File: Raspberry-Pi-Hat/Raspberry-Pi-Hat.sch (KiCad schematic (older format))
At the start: 53 parts, among them J3 40HAT, J6 CONN_02X02, J9 CONN_01X02, Q1 DMG2305UX, Q2 DMMT5401, U2 CAT24C32

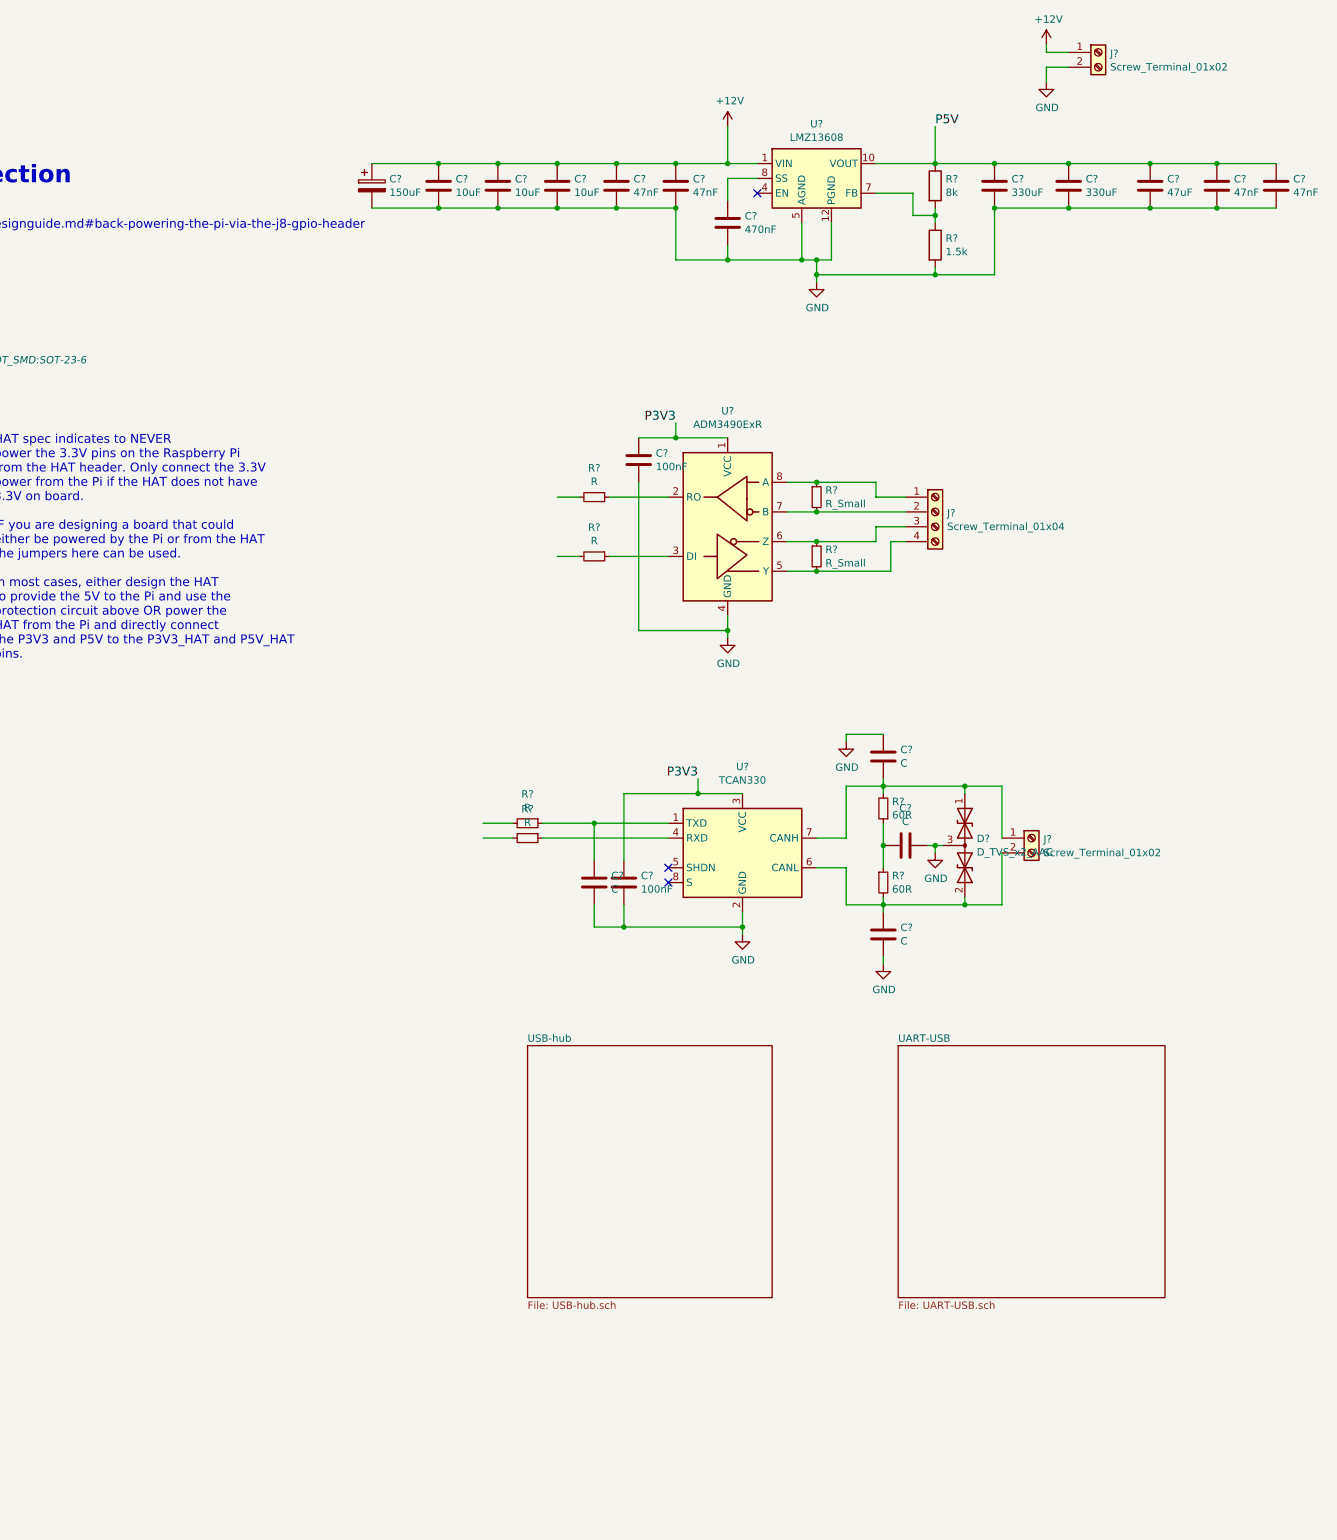
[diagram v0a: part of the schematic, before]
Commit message: USB-HUB
Implementation of USB HUB
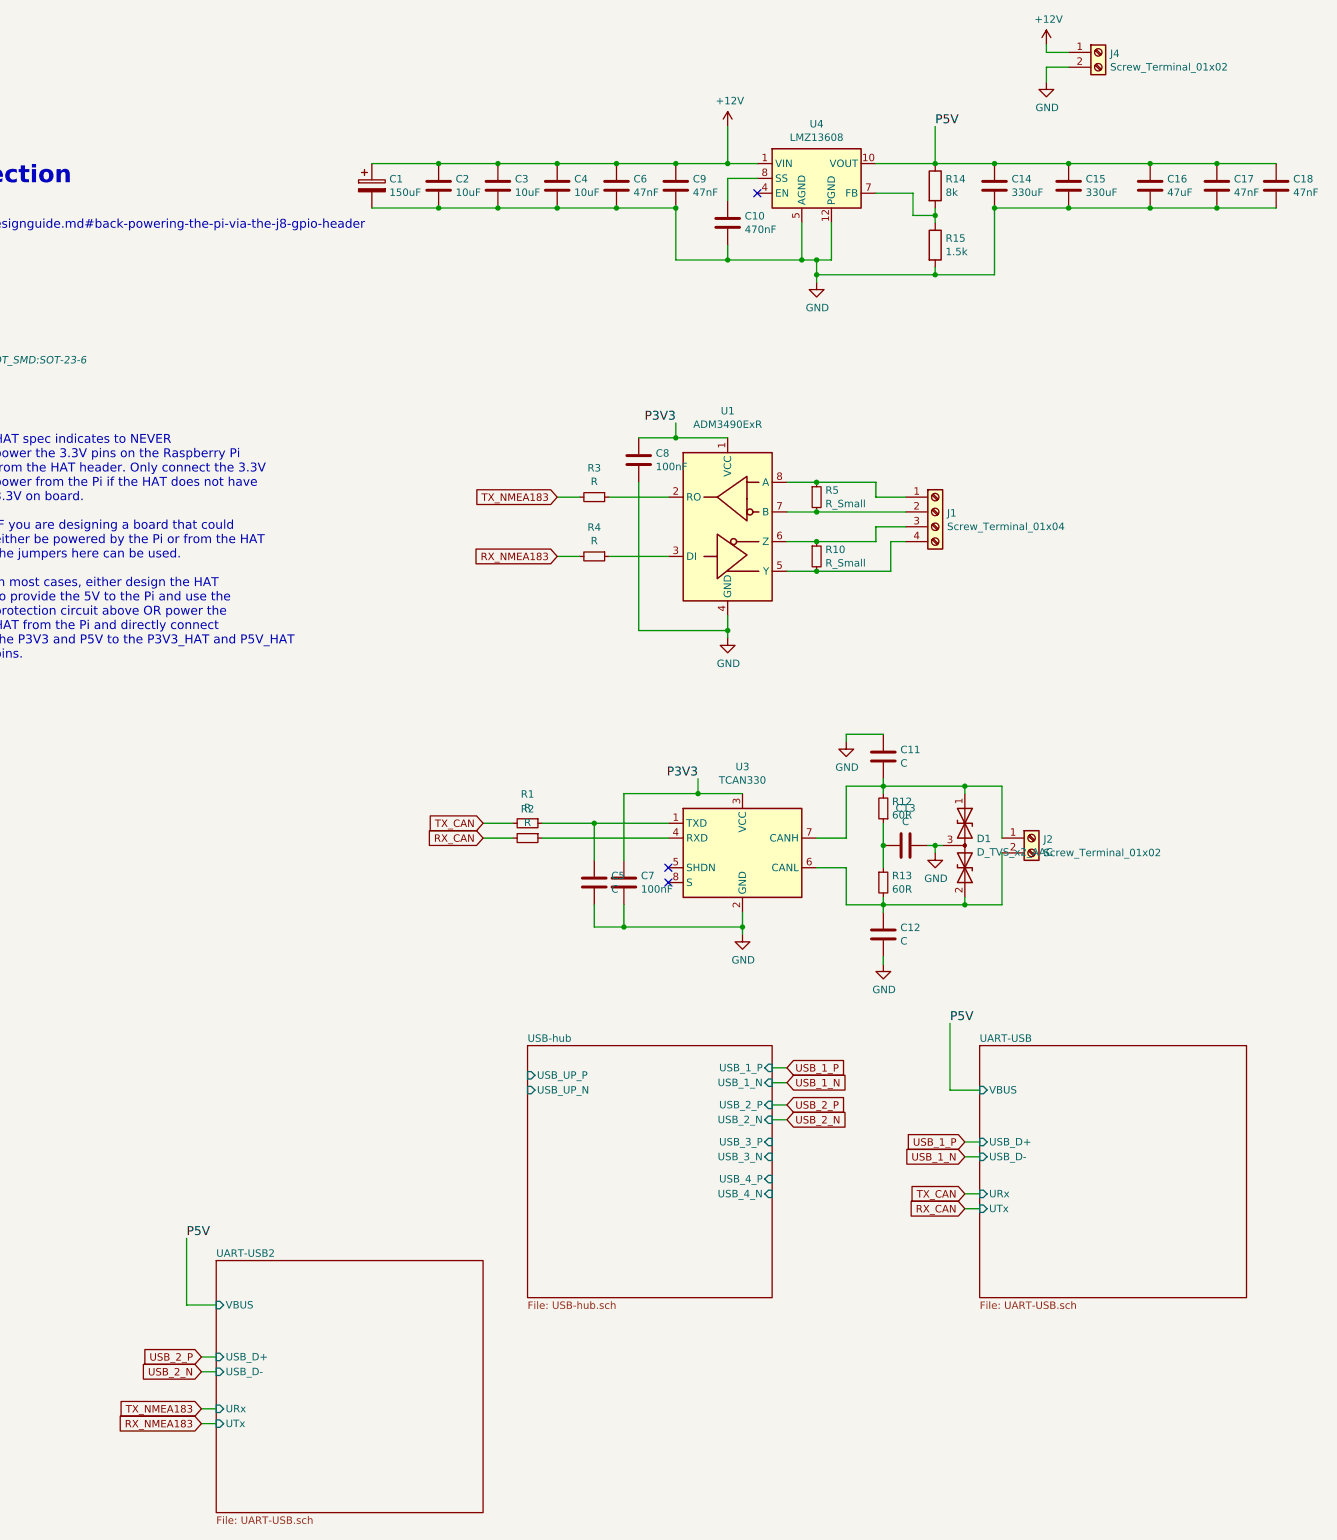
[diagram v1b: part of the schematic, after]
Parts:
- C10, C11, C12, C13, C16, C17, C18, C2, C3, C4, C5, C6, C7, C8, C9: renamed from C?; footprint (none) -> Capacitor_SMD:C_0603_1608Metric_Pad1.05x0.95mm_HandSolder
- gave numbers to parts that had none: 20
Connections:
- net RX_NMEA183: now reaches R4.2
- net TX_NMEA183: now reaches R3.2
- net TX_CAN: now reaches R1.2
- net RX_CAN: now reaches R2.2

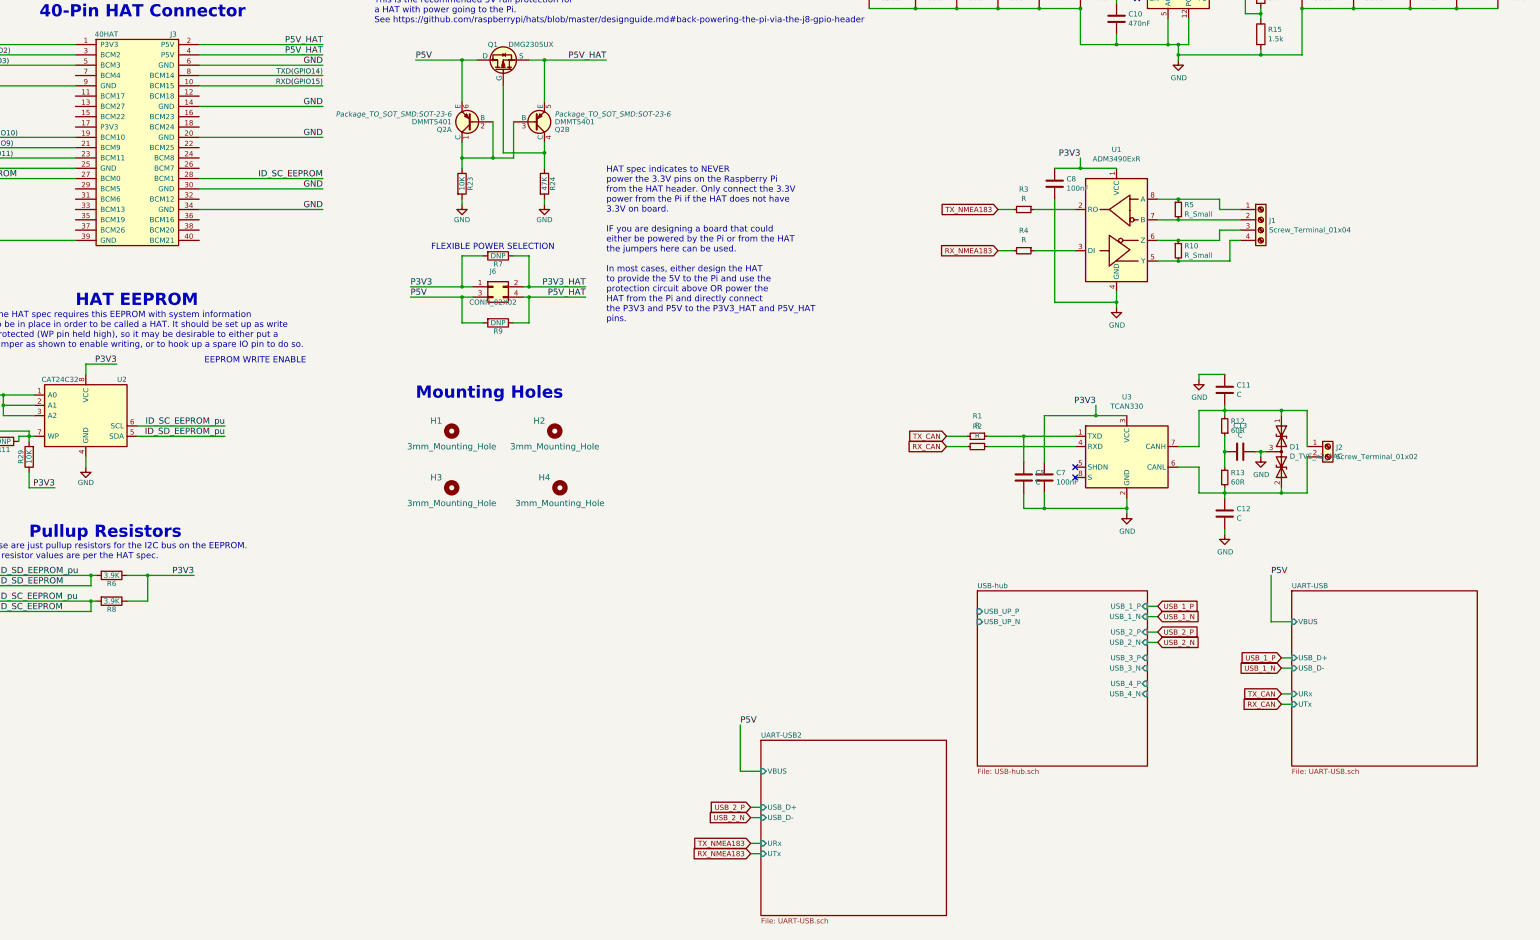
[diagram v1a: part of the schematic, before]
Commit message: Starting placing component
Assigned component footprint and started placing component on the board
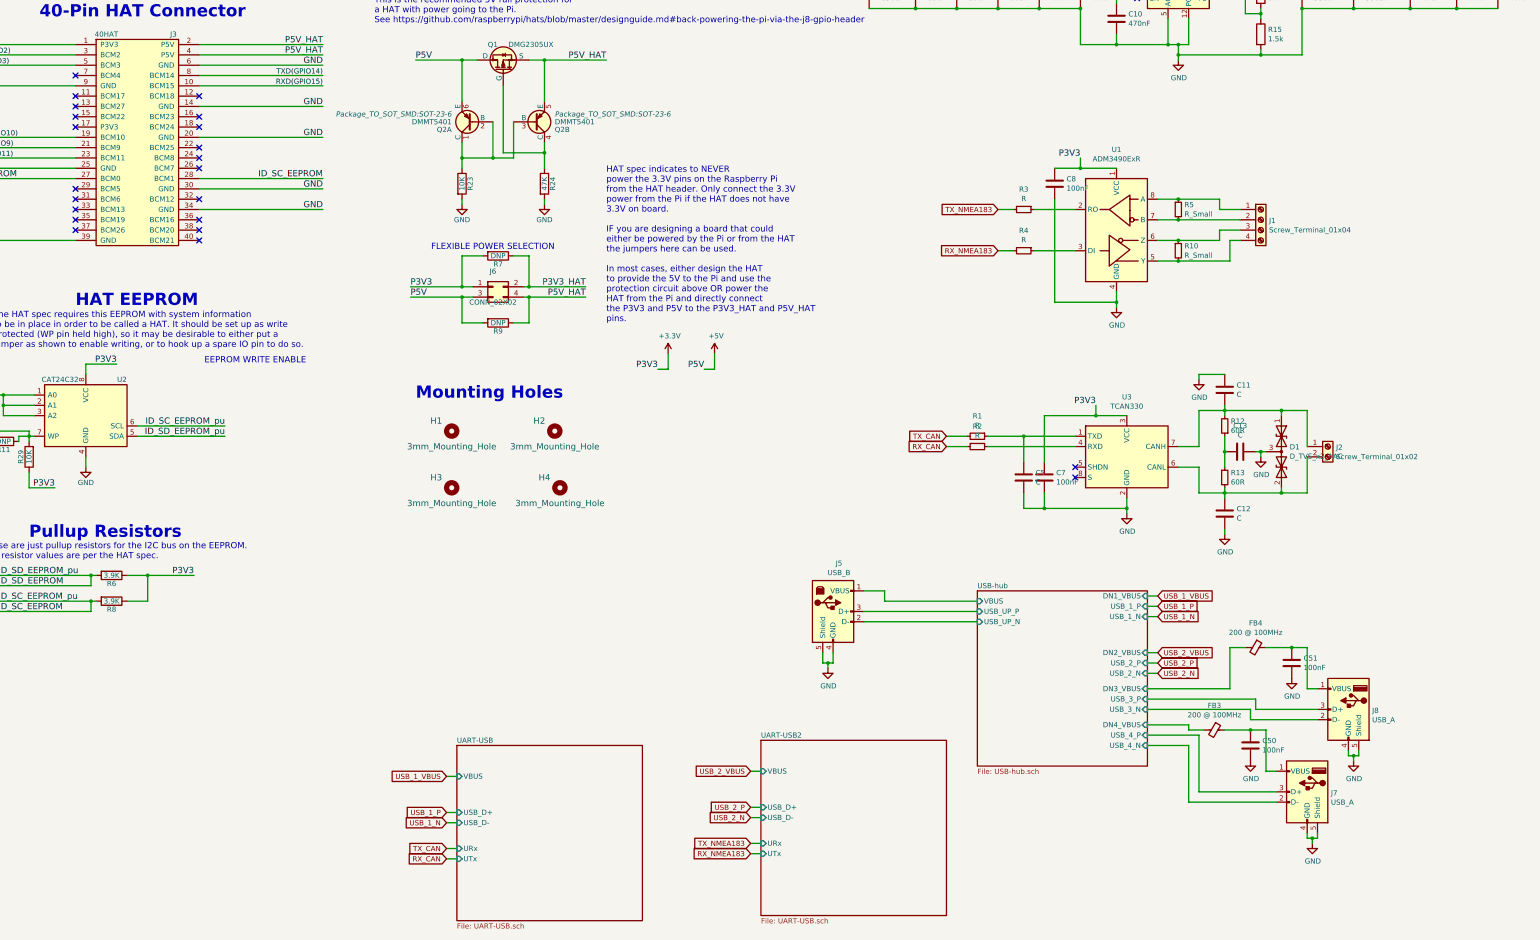
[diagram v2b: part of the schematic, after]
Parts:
- added C50, C51: 100nF, Capacitor_SMD:C_1206_3216Metric_Pad1.42x1.75mm_HandSolder, symbol Device:C
- added FB3, FB4: 200 @ 100MHz, Resistor_SMD:R_0805_2012Metric_Pad1.15x1.40mm_HandSolder, symbol Device:Ferrite_Bead_Small
- added J5: USB_B, Connector_USB:USB_B_Lumberg_2411_02_Horizontal, symbol Connector:USB_B
- added J7, J8: USB_A, Connector_USB:USB_A_Molex_67643_Horizontal, symbol Connector:USB_A
- C1: footprint (none) -> Capacitor_SMD:C_1206_3216Metric_Pad1.42x1.75mm_HandSolder
- C10, C11, C12, C13, C16, C17, C18, C2, C3, C4, C5, C6, C7, C8, C9: footprint Capacitor_SMD:C_0603_1608Metric_Pad1.05x0.95mm_HandSolder -> Capacitor_SMD:C_1206_3216Metric_Pad1.42x1.75mm_HandSolder
- C14: footprint (none) -> Capacitor_Tantalum_SMD:CP_EIA-7343-31_Kemet-D_Pad2.25x2.55mm_HandSolder; Fab (none) -> Kemet; Ref (none) -> T520D337M006ATE015
- C15: footprint (none) -> Capacitor_Tantalum_SMD:CP_EIA-7343-31_Kemet-D_Pad2.25x2.55mm_HandSolder
- D1: footprint (none) -> Package_TO_SOT_SMD:SOT-23; Fab (none) -> Nexperia; Ref (none) -> PESD2ETH100-TR
- J1: footprint (none) -> Connector_Phoenix_MSTB:PhoenixContact_MSTBVA_2,5_4-G-5,08_1x04_P5.08mm_Vertical
- J2, J4: footprint (none) -> Connector_Phoenix_MSTB:PhoenixContact_MSTBVA_2,5_2-G-5,08_1x02_P5.08mm_Vertical
- R1, R10, R2, R3, R4, R5: footprint (none) -> Resistor_SMD:R_1206_3216Metric_Pad1.42x1.75mm_HandSolder
- R12, R13, R14, R15: footprint (none) -> Resistor_SMD:R_0603_1608Metric_Pad1.05x0.95mm_HandSolder
- R29: footprint Resistor_SMD:R_0603_1608Metric_Pad0.84x1.00mm_HandSolder -> Resistor_SMD:R_0603_1608Metric_Pad1.05x0.95mm_HandSolder
- U3: footprint (none) -> Package_TO_SOT_SMD:TSOT-23-8_HandSoldering
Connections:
- net GND: now also C50.1, C51.1, J5.4 (GND), J5.5 (Shield), J7.4 (GND), J7.5 (Shield), J8.4 (GND), J8.5 (Shield)
- net USB-hub/USB_3_N: now also J8.2 (D-)
- net USB-hub/USB_3_P: now also J8.3 (D+)
- net USB-hub/USB_4_N: now also J7.2 (D-)
- net USB-hub/USB_4_P: now also J7.3 (D+)
- net USB-hub/USB_UP_N: now also J5.2 (D-)
- net USB-hub/USB_UP_P: now also J5.3 (D+)
- net P3V3 renamed +3V3
- net P5V renamed +5V
- new net: C51.2, FB4.1, J8.1 (VBUS)
- new net: C50.2, FB3.1, J7.1 (VBUS)
- new net USB-hub/DN3_VBUS: FB4.2
- new net USB-hub/DN4_VBUS: FB3.2
- new net USB-hub/VBUS: J5.1 (VBUS)
- no-connect marks 3 -> 23
